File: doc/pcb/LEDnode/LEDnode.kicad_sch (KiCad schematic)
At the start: 57 parts, among them J1 LI BAT, Q1 BC807, Q2 BC807, Q3 BC807, Q4 BC807, SW1 EC11J12-15P30C-SW, U1 STM32G071KxT, U2 AF-02841BMR-B, U4 AP1603, U5 BME280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

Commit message: almost working menu
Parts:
- added C?: 104, symbol Device:C
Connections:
- net +3V3: now also C?.1
- net GND: now also C?.2
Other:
- moved on the sheet: C?, Q?, R?, SW1

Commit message: working watch
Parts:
- added R?: 0, symbol Device:R
- R? (x3): value 10k -> MCU_INT
- R? (x2): value 10k -> 100k
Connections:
- net +3V3: no longer SW?.3 (C)
- net GND: now also R?.2
- net at Q?.3 (D), SW1.C: now also R?.1
- no-connect marks 2 -> 3
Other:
- note added: "CONRTOL BY MCU"
- note added: "FORCE ACTIVE"
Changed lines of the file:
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@@
   (junction (at 248.285 60.96) (diameter 0) (color 0 0 0 0)
   )
+  (junction (at 57.785 126.365) (diameter 0) (color 0 0 0 0)
+  )
   (junction (at 254.635 20.955) (diameter 0) (color 0 0 0 0)
+  )
+  (junction (at 57.785 106.045) (diameter 0) (color 0 0 0 0)
   )
   (junction (at 46.99 27.94) (diameter 0) (color 0 0 0 0)
@@
   (no_connect (at 268.605 42.545))
   (no_connect (at 268.605 45.085))
+  (no_connect (at 25.4 157.48))
   (wire (pts (xy 74.93 93.98) (xy 77.47 93.98))
     (stroke (width 0) (type default) (color 0 0 0 0))
@@
     (stroke (width 0) (type default) (color 0 0 0 0))
   )
+  (wire (pts (xy 57.785 126.365) (xy 72.39 126.365))
+    (stroke (width 0) (type default) (color 0 0 0 0))
+  )
   (wire (pts (xy 280.67 20.955) (xy 280.67 27.305))
     (stroke (width 0) (type default) (color 0 0 0 0))
@@
     (stroke (width 0) (type default) (color 0 0 0 0))
   )
-  (wire (pts (xy 57.785 125.095) (xy 57.785 127.635))
+  (wire (pts (xy 57.785 125.095) (xy 57.785 126.365))
     (stroke (width 0) (type default) (color 0 0 0 0))
   )
@@
     (stroke (width 0) (type default) (color 0 0 0 0))
   )
-  (wire (pts (xy 20.32 157.48) (xy 25.4 157.48))
-    (stroke (width 0) (type default) (color 0 0 0 0))
-  )
   (wire (pts (xy 36.83 27.94) (xy 41.275 27.94))
     (stroke (width 0) (type default) (color 0 0 0 0))
@@
     (stroke (width 0) (type default) (color 0 0 0 0))
   )
+  (wire (pts (xy 72.39 106.045) (xy 57.785 106.045))
+    (stroke (width 0) (type default) (color 0 0 0 0))
+  )
   (wire (pts (xy 160.655 41.91) (xy 161.925 41.91))
     (stroke (width 0) (type default) (color 0 0 0 0))
@@
     (stroke (width 0) (type default) (color 0 0 0 0))
   )
+  (wire (pts (xy 72.39 106.045) (xy 72.39 116.205))
+    (stroke (width 0) (type default) (color 0 0 0 0))
+  )
   (wire (pts (xy 183.515 26.035) (xy 183.515 24.765))
     (stroke (width 0) (type default) (color 0 0 0 0))
@@
     (stroke (width 0) (type default) (color 0 0 0 0))
   )
+  (wire (pts (xy 57.785 126.365) (xy 57.785 127.635))
+    (stroke (width 0) (type default) (color 0 0 0 0))
+  )
   (wire (pts (xy 46.99 19.685) (xy 59.055 19.685))
     (stroke (width 0) (type default) (color 0 0 0 0))
@@
     (stroke (width 0) (type default) (color 0 0 0 0))
   )
+  (wire (pts (xy 57.785 106.045) (xy 57.785 114.935))
+    (stroke (width 0) (type default) (color 0 0 0 0))
+  )
+  (wire (pts (xy 72.39 126.365) (xy 72.39 123.825))
+    (stroke (width 0) (type default) (color 0 0 0 0))
+  )
   (wire (pts (xy 266.065 127) (xy 269.24 127))
     (stroke (width 0) (type default) (color 0 0 0 0))
@@
     (stroke (width 0) (type default) (color 0 0 0 0))
   )
-  (wire (pts (xy 57.785 96.52) (xy 57.785 114.935))
+  (wire (pts (xy 57.785 96.52) (xy 57.785 106.045))
     (stroke (width 0) (type default) (color 0 0 0 0))
   )
@@
     (stroke (width 0) (type default) (color 0 0 0 0))
   )
-  (wire (pts (xy 20.32 156.21) (xy 20.32 157.48))
-    (stroke (width 0) (type default) (color 0 0 0 0))
-  )
   (wire (pts (xy 233.045 50.165) (xy 233.045 47.625))
     (stroke (width 0) (type default) (color 0 0 0 0))
@@
   (wire (pts (xy 19.685 27.94) (xy 26.67 27.94))
     (stroke (width 0) (type default) (color 0 0 0 0))
+  )
+  (text "FORCE ACTIVE" (at 69.85 125.73 90)
+    (effects (font (size 1.27 1.27)) (justify left bottom))
+  )
+  (text "CONRTOL BY MCU" (at 62.23 126.365 90)
+    (effects (font (size 1.27 1.27)) (justify left bottom))
   )
   (label "BUTTON1" (at 175.895 93.345 0)
@@
   )
   (symbol (lib_id "Device:R") (at 48.26 153.67 0) (unit 1)
-    (in_bom yes) (on_board yes) (fields_autoplaced)
-    (property "Reference" "R?" (id 0) (at 50.038 152.8353 0)
-      (effects (font (size 1.27 1.27)) (justify left))
-    )
-    (property "Value" "10k" (id 1) (at 50.038 155.3722 0)
+    (in_bom yes) (on_board yes)
+    (property "Reference" "R?" (id 0) (at 41.275 153.035 0)
+      (effects (font (size 1.27 1.27)) (justify left))
+    )
+    (property "Value" "MCU_INT" (id 1) (at 41.275 154.94 0)
       (effects (font (size 1.27 1.27)) (justify left))
     )
@@
       (effects (font (size 1.27 1.27)) (justify left))
     )
-    (property "Value" "10k" (id 1) (at 56.388 155.3722 0)
+    (property "Value" "MCU_INT" (id 1) (at 56.388 155.3722 0)
       (effects (font (size 1.27 1.27)) (justify left))
     )
@@
       (effects (font (size 1.27 1.27)) (justify left))
     )
-    (property "Value" "10k" (id 1) (at 40.005 88.9 0)
+    (property "Value" "100k" (id 1) (at 38.735 90.17 0)
       (effects (font (size 1.27 1.27)) (justify left))
     )
@@
     (in_bom yes) (on_board yes)
     (property "Reference" "R?" (id 0) (at 31.115 88.265 0))
-    (property "Value" "10k" (id 1) (at 31.115 90.805 0))
+    (property "Value" "100k" (id 1) (at 31.115 90.805 0))
     (property "Footprint" "" (id 2) (at 33.147 89.535 90)
       (effects (font (size 1.27 1.27)) hide)
@@
       (effects (font (size 1.27 1.27)) (justify left))
     )
-    (property "Value" "10k" (id 1) (at 87.503 89.3322 0)
+    (property "Value" "MCU_INT" (id 1) (at 87.503 89.3322 0)
       (effects (font (size 1.27 1.27)) (justify left))
     )
@@
     (pin "2")
     (pin "3")
-  )
-  (symbol (lib_id "power:+3V3") (at 20.32 156.21 0) (unit 1)
-    (in_bom yes) (on_board yes) (fields_autoplaced)
-    (property "Reference" "#PWR?" (id 0) (at 20.32 160.02 0)
-      (effects (font (size 1.27 1.27)) hide)
-    )
-    (property "Value" "+3V3" (id 1) (at 20.32 152.6342 0))
-    (property "Footprint" "" (id 2) (at 20.32 156.21 0)
-      (effects (font (size 1.27 1.27)) hide)
-    )
-    (property "Datasheet" "" (id 3) (at 20.32 156.21 0)
-      (effects (font (size 1.27 1.27)) hide)
-    )
-    (pin "1")
   )
   (symbol (lib_id "power:+3V3") (at 194.945 150.495 0) (unit 1)
@@
     )
     (property "Datasheet" "~" (id 3) (at 128.27 36.195 0)
+      (effects (font (size 1.27 1.27)) hide)
+    )
+    (pin "1")
+    (pin "2")
+  )
+  (symbol (lib_id "Device:R") (at 72.39 120.015 0) (unit 1)
+    (in_bom yes) (on_board yes) (fields_autoplaced)
+    (property "Reference" "R?" (id 0) (at 74.168 119.1803 0)
+      (effects (font (size 1.27 1.27)) (justify left))
+    )
+    (property "Value" "0" (id 1) (at 74.168 121.7172 0)
+      (effects (font (size 1.27 1.27)) (justify left))
+    )
+    (property "Footprint" "" (id 2) (at 70.612 120.015 90)
+      (effects (font (size 1.27 1.27)) hide)
+    )
+    (property "Datasheet" "~" (id 3) (at 72.39 120.015 0)
       (effects (font (size 1.27 1.27)) hide)
     )
@@
   )
   (symbol (lib_id "Device:Q_NMOS_GSD") (at 55.245 120.015 0) (unit 1)
-    (in_bom yes) (on_board yes) (fields_autoplaced)
-    (property "Reference" "Q?" (id 0) (at 60.452 119.1803 0)
-      (effects (font (size 1.27 1.27)) (justify left))
-    )
-    (property "Value" "BSS138" (id 1) (at 60.452 121.7172 0)
+    (in_bom yes) (on_board yes)
+    (property "Reference" "Q?" (id 0) (at 52.705 116.205 0)
+      (effects (font (size 1.27 1.27)) (justify left))
+    )
+    (property "Value" "BSS138" (id 1) (at 48.26 125.095 0)
       (effects (font (size 1.27 1.27)) (justify left))
     )
@@
   )
   (symbol (lib_id "Device:R") (at 42.545 160.02 90) (unit 1)
-    (in_bom yes) (on_board yes) (fields_autoplaced)
-    (property "Reference" "R?" (id 0) (at 42.545 155.3042 90))
-    (property "Value" "220R" (id 1) (at 42.545 157.8411 90))
+    (in_bom yes) (on_board yes)
+    (property "Reference" "R?" (id 0) (at 41.91 157.48 90))
+    (property "Value" "220R" (id 1) (at 41.91 162.56 90))
     (property "Footprint" "" (id 2) (at 42.545 161.798 90)
       (effects (font (size 1.27 1.27)) hide)
@@
       (reference "#PWR?") (unit 1) (value "GND") (footprint "")
     )
-    (path "/b11c17d4-1689-44b1-b523-42bc94c085cb"
-      (reference "#PWR?") (unit 1) (value "+3V3") (footprint "")
-    )
     (path "/c8dff9bf-d419-48ba-b30c-2443078f973b"
       (reference "#PWR?") (unit 1) (value "GND") (footprint "")
@@
     )
     (path "/3f6b748f-cbfb-4dd8-8e5d-2f98bc56dc7c"
-      (reference "R?") (unit 1) (value "10k") (footprint "")
+      (reference "R?") (unit 1) (value "MCU_INT") (footprint "")
     )
     (path "/490bd2c9-43de-4be7-92ea-5d5d3a884837"
@@
     )
     (path "/4b020f2d-2586-4ff5-8a8c-2009cf86c195"
-      (reference "R?") (unit 1) (value "10k") (footprint "")
+      (reference "R?") (unit 1) (value "MCU_INT") (footprint "")
     )
     (path "/6758fe33-c8d5-4407-9f16-c72d8affd56a"
-      (reference "R?") (unit 1) (value "10k") (footprint "")
+      (reference "R?") (unit 1) (value "100k") (footprint "")
     )
     (path "/90f62ab4-3b57-4e43-92c1-505510d0ded2"
-      (reference "R?") (unit 1) (value "10k") (footprint "")
+      (reference "R?") (unit 1) (value "100k") (footprint "")
     )
     (path "/a1456448-0362-4548-a09f-83bda68ee060"
-      (reference "R?") (unit 1) (value "10k") (footprint "")
+      (reference "R?") (unit 1) (value "MCU_INT") (footprint "")
     )
     (path "/c47cf178-6292-46ff-84f3-519ec9127e98"
@@
       (reference "R?") (unit 1) (value "220R") (footprint "")
     )
+    (path "/c629dfaa-37af-4767-afa6-bfe5d03347b7"
+      (reference "R?") (unit 1) (value "0") (footprint "")
+    )
     (path "/d45eddae-f4fa-4533-9388-fd4214b0f80e"

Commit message: working clock set
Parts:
- added R?: 1k, symbol Device:R
- R? (x2): value 100k -> 10k
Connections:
- net ENCODER_ACTIVE: now also R?.1; no longer Q?.1 (G)
- new net: Q?.1 (G), R?.2
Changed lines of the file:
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@@
     (effects (font (size 1.27 1.27)) (justify right bottom))
   )
-  (label "ENCODER_ACTIVE" (at 50.165 120.015 180)
+  (label "ENCODER_ACTIVE" (at 42.545 120.015 180)
     (effects (font (size 1.27 1.27)) (justify right bottom))
   )
@@
     )
     (property "Datasheet" "~" (id 3) (at 114.935 38.1 0)
+      (effects (font (size 1.27 1.27)) hide)
+    )
+    (pin "1")
+    (pin "2")
+  )
+  (symbol (lib_id "Device:R") (at 46.355 120.015 90) (unit 1)
+    (in_bom yes) (on_board yes) (fields_autoplaced)
+    (property "Reference" "R?" (id 0) (at 46.355 115.2992 90))
+    (property "Value" "1k" (id 1) (at 46.355 117.8361 90))
+    (property "Footprint" "" (id 2) (at 46.355 121.793 90)
+      (effects (font (size 1.27 1.27)) hide)
+    )
+    (property "Datasheet" "~" (id 3) (at 46.355 120.015 0)
       (effects (font (size 1.27 1.27)) hide)
     )
@@
       (effects (font (size 1.27 1.27)) (justify left))
     )
-    (property "Value" "100k" (id 1) (at 38.735 90.17 0)
+    (property "Value" "10k" (id 1) (at 38.735 90.17 0)
       (effects (font (size 1.27 1.27)) (justify left))
     )
@@
     (in_bom yes) (on_board yes)
     (property "Reference" "R?" (id 0) (at 31.115 88.265 0))
-    (property "Value" "100k" (id 1) (at 31.115 90.805 0))
+    (property "Value" "10k" (id 1) (at 31.115 90.805 0))
     (property "Footprint" "" (id 2) (at 33.147 89.535 90)
       (effects (font (size 1.27 1.27)) hide)
@@
       (reference "R?") (unit 1) (value "220") (footprint "")
     )
+    (path "/21fe163d-5c16-42b5-8408-6e6165b7b3e7"
+      (reference "R?") (unit 1) (value "1k") (footprint "")
+    )
     (path "/3cf880b3-5c9a-41b3-9cf9-9a6d06aa346b"
       (reference "R?") (unit 1) (value "220") (footprint "")
@@
     )
     (path "/6758fe33-c8d5-4407-9f16-c72d8affd56a"
-      (reference "R?") (unit 1) (value "100k") (footprint "")
+      (reference "R?") (unit 1) (value "10k") (footprint "")
     )
     (path "/90f62ab4-3b57-4e43-92c1-505510d0ded2"
-      (reference "R?") (unit 1) (value "100k") (footprint "")
+      (reference "R?") (unit 1) (value "10k") (footprint "")
     )
     (path "/a1456448-0362-4548-a09f-83bda68ee060"

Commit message: ...
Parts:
- removed J1: LI BAT, BartLib_Battery:BC-0401 AAA R3, symbol Connector:Conn_01x02_Female
- added J1: Ni-MH, BartLib_Battery:BC-0401 AAA R3, symbol Connector:Conn_01x02_Male
- C15, C16, C17, C18, C19, C20: renamed from C?; footprint (none) -> Capacitor_SMD:C_0603_1608Metric
- D1: renamed from D?; footprint (none) -> Diode_SMD:D_SOD-123
- D2, D3: renamed from D?; footprint (none) -> LED_SMD:LED_0603_1608Metric
- J2: renamed from J?; footprint (none) -> Connector_PinHeader_1.27mm:PinHeader_1x05_P1.27mm_Vertical
- J3: renamed from J?; footprint (none) -> Connector_PinHeader_2.54mm:PinHeader_1x06_P2.54mm_Vertical
- J4: renamed from J?; footprint (none) -> Connector_PinHeader_2.54mm:PinHeader_1x08_P2.54mm_Vertical
- Q5, Q6: renamed from Q?; footprint (none) -> Package_TO_SOT_SMD:SOT-23
- R1, R10, R11, R12, R13, R14, R15, R16, R17, R2, R6, R7, R8, R9: renamed from R?; footprint (none) -> Resistor_SMD:R_0603_1608Metric
- SW2: renamed from SW?; value SW_SPDT -> MFP 120; footprint (none) -> BartLib_Switch:MFP 120
- SW3: renamed from SW?; value SW_SPST -> TL3342F160QG; footprint (none) -> Button_Switch_SMD:SW_SPST_B3SL-1002P
- U2: footprint BartLib_Display:LED 7.2mm -> BartLib_Display:LED 7.2mm SMD
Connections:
- net INPUT: now also J1.1 (Pin_1)
- net at D1.1 (K), Q5.3 (D): now also J1.2 (Pin_2)

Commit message: working chronograph, designed PCB
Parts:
- added H1, H2, H3, H4: MountingHole_Pad, BartLib_Pad:WirePad 4mm^2 Rect, symbol Mechanical:MountingHole_Pad
- C13: value C -> 104
- C2, C5: value 107 -> 476; footprint Capacitor_THT:CP_Radial_D8.0mm_P3.50mm -> Capacitor_SMD:CP_Elec_5x4.5
- Y1: footprint Crystal:Crystal_C26-LF_D2.1mm_L6.5mm_Horizontal_1EP_style1 -> Crystal:Crystal_C26-LF_D2.1mm_L6.5mm_Horizontal
- renumbered C14 to C105
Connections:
- net DISP_4 is gone; now on net DISP_3: Q4.1 (B)
- net DISP_0: now also J4.2 (Pin_2), Q1.1 (B), U1.13 (PA6); no longer U1.20 (PC6)
- net DISP_1: now also Q2.1 (B), U1.16 (PB1); no longer Q1.1 (B), U1.23 (PA12_[PA10])
- net DISP_2: now also Q3.1 (B), U1.17 (PB2); no longer Q2.1 (B), U1.26 (PA15)
- net DISP_3: now also U1.19 (PA9); no longer J4.3 (Pin_3), Q3.1 (B), U1.14 (PA7)
- net DISP_A: now also J4.3 (Pin_3), U1.14 (PA7); no longer U1.21 (PA10)
- net DISP_B: now also J4.4 (Pin_4), U1.18 (PA8); no longer J4.2 (Pin_2), U1.13 (PA6)
- net DISP_C: now also U1.23 (PA12_[PA10]); no longer U1.16 (PB1)
- net DISP_D: now also U1.21 (PA10); no longer J4.4 (Pin_4), U1.18 (PA8)
- net DISP_DP: now also U1.22 (PA11_[PA9]); no longer U1.19 (PA9)
- net DISP_E: now also U1.20 (PC6); no longer U1.17 (PB2)
- net DISP_F: now also J4.5 (Pin_5), U1.15 (PB0); no longer U1.22 (PA11_[PA9])
- net DISP_G: now also U1.26 (PA15); no longer J4.5 (Pin_5), U1.15 (PB0)
- net GND: now also H1.1, H2.1, H3.1, H4.1

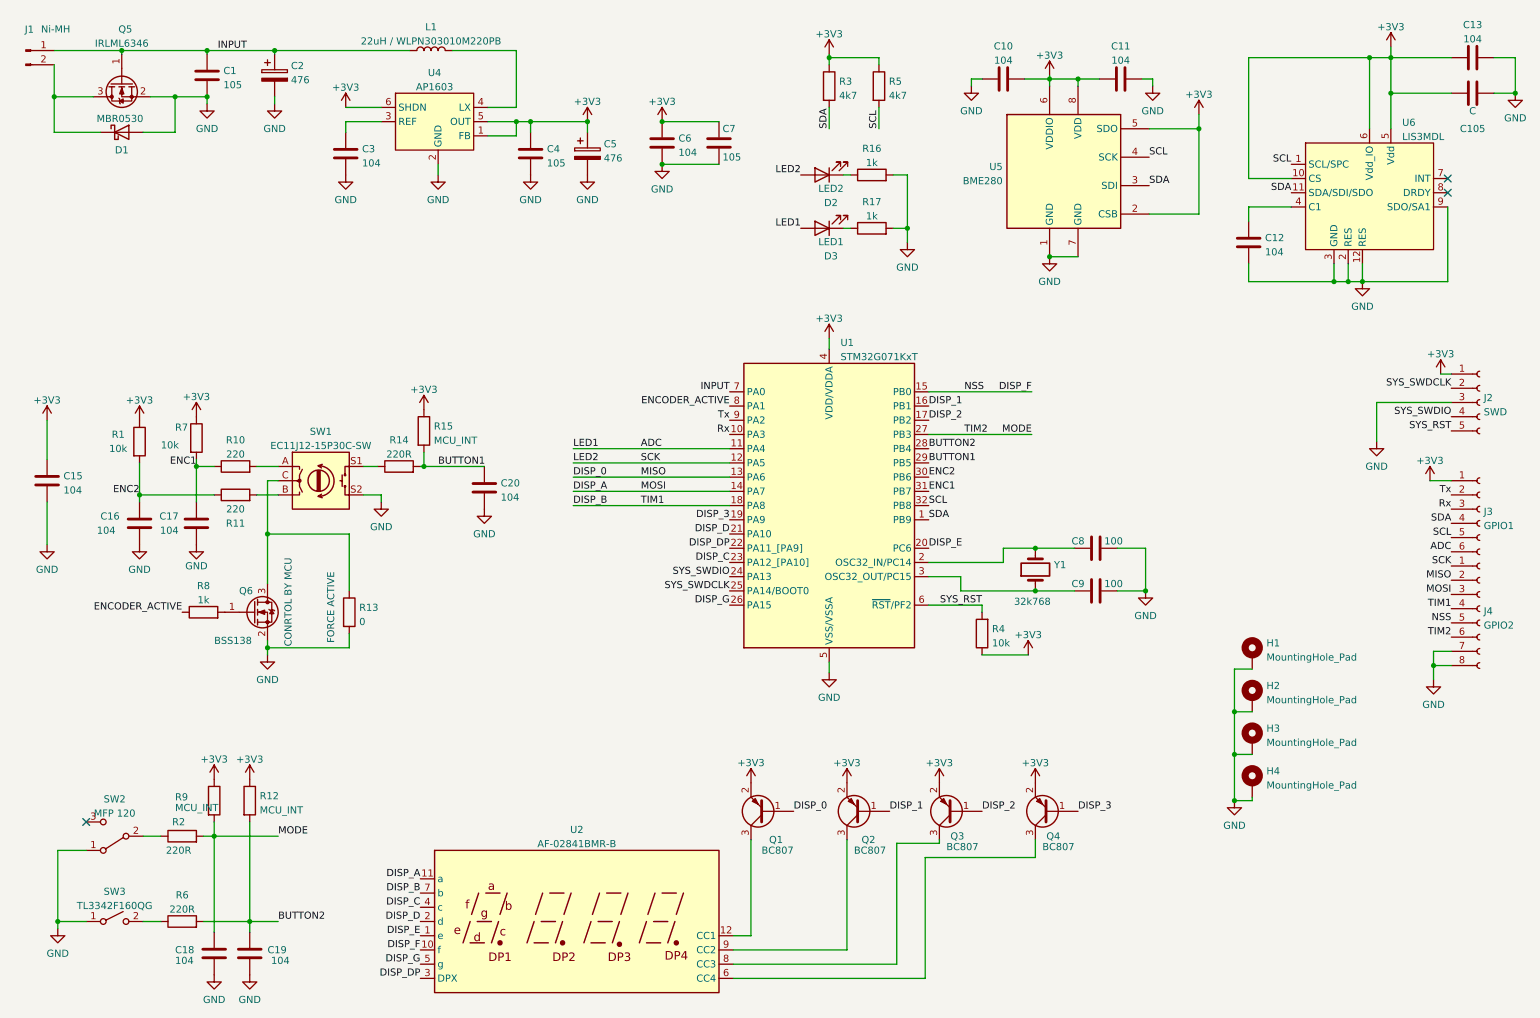
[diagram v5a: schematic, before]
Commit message: added segment resistors
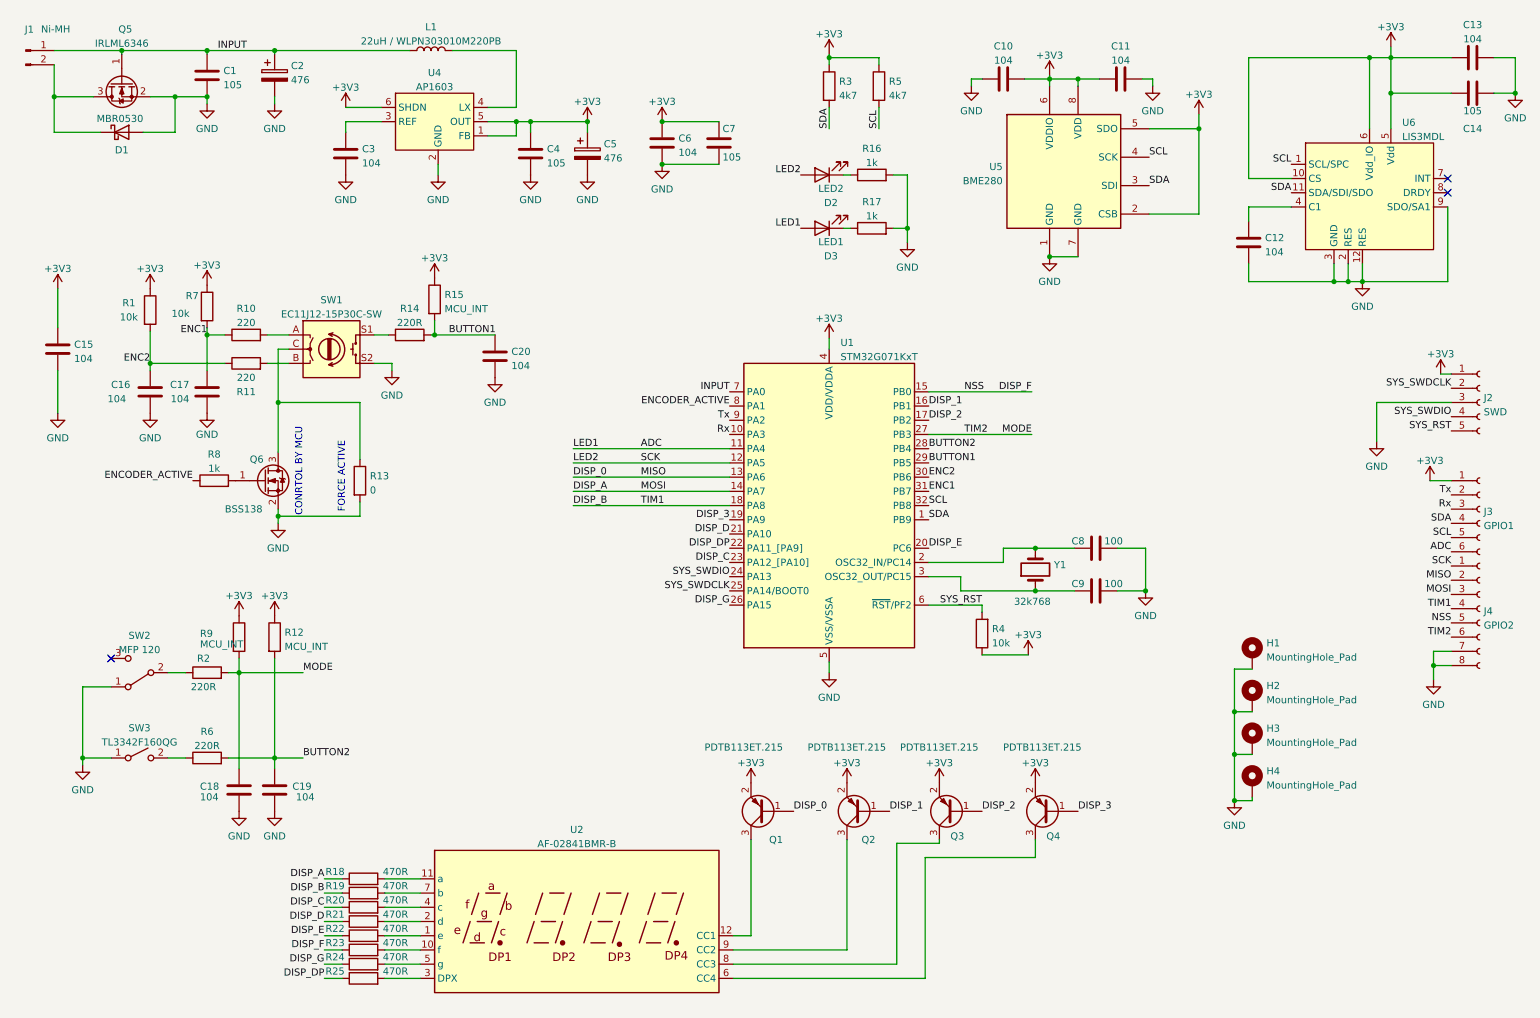
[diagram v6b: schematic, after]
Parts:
- added R18, R19, R20, R21, R22, R23, R24, R25: 470R, Resistor_SMD:R_0603_1608Metric, symbol Device:R
- C14: renamed from C105; value C -> 105
- Q1, Q2, Q3, Q4: value BC807 -> PDTB113ET.215
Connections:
- net DISP_A: now also R18.1; no longer U2.11 (a)
- net DISP_B: now also R19.1; no longer U2.7 (b)
- net DISP_C: now also R20.1; no longer U2.4 (c)
- net DISP_D: now also R21.1; no longer U2.2 (d)
- net DISP_DP: now also R25.1; no longer U2.3 (DPX)
- net DISP_E: now also R22.1; no longer U2.1 (e)
- net DISP_F: now also R23.1; no longer U2.10 (f)
- net DISP_G: now also R24.1; no longer U2.5 (g)
- new net: R19.2, U2.7 (b)
- new net: R22.2, U2.1 (e)
- new net: R23.2, U2.10 (f)
- new net: R18.2, U2.11 (a)
- new net: R21.2, U2.2 (d)
- new net: R25.2, U2.3 (DPX)
- new net: R20.2, U2.4 (c)
- new net: R24.2, U2.5 (g)
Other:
- moved on the sheet: C15, C16, C17, C18, C19, C20, Q6, R1, R10, R11, R12, R13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
